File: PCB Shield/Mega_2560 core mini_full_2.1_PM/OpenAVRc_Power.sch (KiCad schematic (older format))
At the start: 18 parts, among them P17 BATT, P21 Sw_power, P26 LCD_Alim, P29 Sw_On, P30 MiniDCDC3A, U4 PM5033, U5 LD1117S33TR

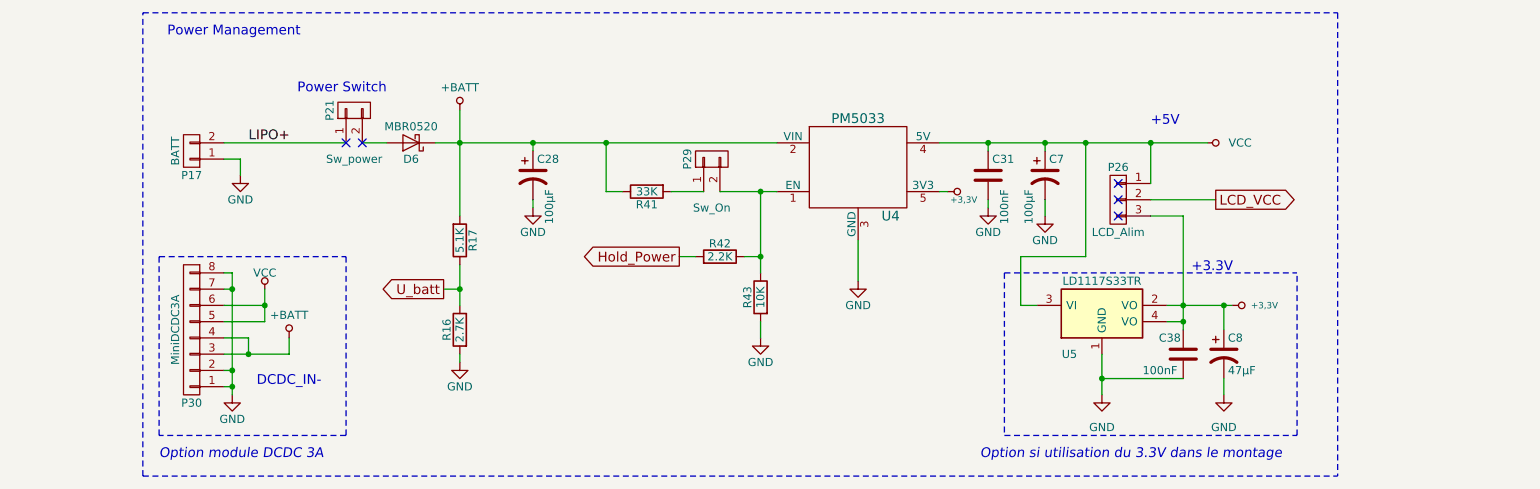
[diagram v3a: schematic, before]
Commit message: Update schematic & pcb files
add mosfet function
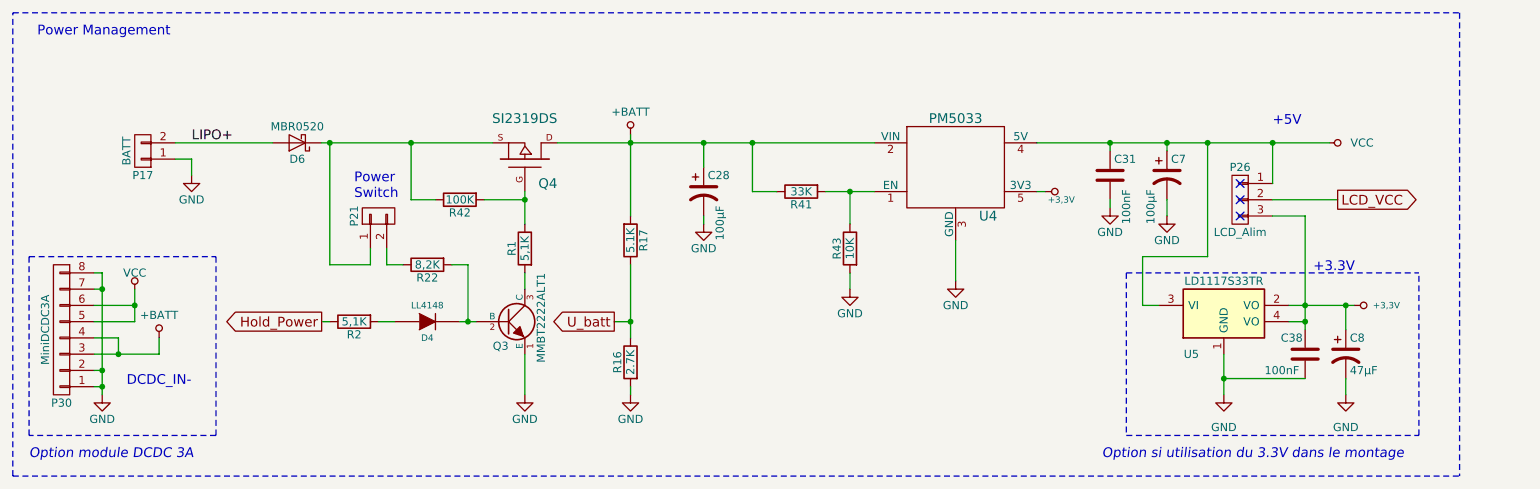
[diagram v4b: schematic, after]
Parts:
- removed P29: Sw_On, Pin_Headers:Pin_Header_Straight_1x02_Pitch2.54mm, symbol CONN_01X02
- added D4: LL4148, Diodes_SMD:D_SOD-123, symbol DIODE
- added Q3: MMBT2222ALT1, SOT-23_MMBT2222, symbol NPN
- added Q4: SI2319DS, SOT-23_MOS_P, symbol MOS_P
- added R1, R2: 5,1K, Resistors_SMD:R_1206, symbol R-RESCUE-Mega_2560_core_mini_full_2.0
- added R22: 8,2K, Resistors_SMD:R_1206, symbol R-RESCUE-Mega_2560_core_mini_full_2.0
- R42: value 2.2K -> 100K
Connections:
- net +BATT: now also Q4.D; no longer D6.1 (K)
- net GND: now also Q3.1 (E)
- net Hold_Power: now also R2.1; no longer R42.2
- net LIPO+: now also D6.2 (A); no longer P21.1 (P1)
- net at P21.2 (P2): now also R22.1; no longer D6.2 (A)
- net at R43.1, U4.1 (EN): now also R41.2; no longer R42.1
- new net: D6.1 (K), P21.1 (P1), Q4.S, R42.1
- new net: Q4.G, R1.1, R42.2
- new net: D4.2 (K), Q3.2 (B), R22.2
- new net: Q3.3 (C), R1.2
- new net: D4.1 (A), R2.2
- no-connect marks 5 -> 3
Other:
- note added: "Power\nSwitch"
- note removed: "Power Switch"
- moved on the sheet: C28, C31, C38, C7, C8, D6, P17, P21, P26, P30, R16, R17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

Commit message: Update pcb shield
Update core component (change pin 99 from GND to AGND).
Remove GND on AGND pin.
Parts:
- P30: footprint MiniDCDC3A -> v2.1:MiniDCDC3A
- Q3: footprint SOT-23_MMBT2222 -> v2.1:SOT-23_MMBT2222
- Q4: footprint SOT-23_MOS_P -> v2.1:SOT-23_MOS_P
- U4: footprint PM5033_SIL5 -> v2.1:Pm5033_sil5
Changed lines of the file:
@@
 Sheet 7 7
 Title "Shield Mega2560 core Full"
-Date "2018-04-19"
+Date "2018-04-25"
 Rev "2.10"
 Comp "© Team OpenAVRc"
@@
 $EndComp
 $Comp
-L GND-RESCUE-Mega_2560_core_mini_full_2.0 #PWR0110
+L GND-RESCUE-Mega_2560_core_mini_full_2.0 #PWR0109
 U 1 1 59C5313F
 P 8950 4550
-F 0 "#PWR0110" H 8950 4300 50  0001 C CNN
+F 0 "#PWR0109" H 8950 4300 50  0001 C CNN
 F 1 "GND" H 8950 4350 50  0000 C CNN
 F 2 "" H 8950 4550 50  0000 C CNN
@@
 +5V
 $Comp
-L VCC #PWR0111
+L VCC #PWR0110
 U 1 1 59C5314F
 P 9600 3000
-F 0 "#PWR0111" H 9600 2850 50  0001 C CNN
+F 0 "#PWR0110" H 9600 2850 50  0001 C CNN
 F 1 "VCC" V 9600 3200 50  0000 C CNN
 F 2 "" H 9600 3000 50  0000 C CNN
@@
 Power Management
 $Comp
-L GND-RESCUE-Mega_2560_core_mini_full_2.0 #PWR0112
+L GND-RESCUE-Mega_2560_core_mini_full_2.0 #PWR0111
 U 1 1 59C5315D
 P 7300 3850
-F 0 "#PWR0112" H 7300 3600 50  0001 C CNN
+F 0 "#PWR0111" H 7300 3600 50  0001 C CNN
 F 1 "GND" H 7300 3700 50  0000 C CNN
 F 2 "" H 7300 3850 50  0000 C CNN
@@
 $EndComp
 $Comp
-L GND-RESCUE-Mega_2560_core_mini_full_2.0 #PWR0113
+L GND-RESCUE-Mega_2560_core_mini_full_2.0 #PWR0112
 U 1 1 59C53163
 P 5300 4550
-F 0 "#PWR0113" H 5300 4300 50  0001 C CNN
+F 0 "#PWR0112" H 5300 4300 50  0001 C CNN
 F 1 "GND" H 5300 4400 50  0000 C CNN
 F 2 "" H 5300 4550 50  0000 C CNN
@@
 $EndComp
 $Comp
-L GND-RESCUE-Mega_2560_core_mini_full_2.0 #PWR0114
+L GND-RESCUE-Mega_2560_core_mini_full_2.0 #PWR0113
 U 1 1 59C53189
 P 8250 3400
-F 0 "#PWR0114" H 8250 3150 50  0001 C CNN
+F 0 "#PWR0113" H 8250 3150 50  0001 C CNN
 F 1 "GND" H 8250 3250 50  0000 C CNN
 F 2 "" H 8250 3400 50  0000 C CNN
@@
 $EndComp
 $Comp
-L GND-RESCUE-Mega_2560_core_mini_full_2.0 #PWR0115
+L GND-RESCUE-Mega_2560_core_mini_full_2.0 #PWR0114
 U 1 1 59C53196
 P 5750 3500
-F 0 "#PWR0115" H 5750 3250 50  0001 C CNN
+F 0 "#PWR0114" H 5750 3250 50  0001 C CNN
 F 1 "GND" H 5750 3350 50  0000 C CNN
 F 2 "" H 5750 3500 50  0000 C CNN
@@
 $EndComp
 $Comp
-L GND-RESCUE-Mega_2560_core_mini_full_2.0 #PWR0116
+L GND-RESCUE-Mega_2560_core_mini_full_2.0 #PWR0115
 U 1 1 59C531AC
 P 8600 3450
-F 0 "#PWR0116" H 8600 3200 50  0001 C CNN
+F 0 "#PWR0115" H 8600 3200 50  0001 C CNN
 F 1 "GND" H 8600 3300 50  0000 C CNN
 F 2 "" H 8600 3450 50  0000 C CNN
@@
 $EndComp
 $Comp
-L GND-RESCUE-Mega_2560_core_mini_full_2.0 #PWR0117
+L GND-RESCUE-Mega_2560_core_mini_full_2.0 #PWR0116
 U 1 1 59C531B9
 P 9700 4550
-F 0 "#PWR0117" H 9700 4300 50  0001 C CNN
+F 0 "#PWR0116" H 9700 4300 50  0001 C CNN
 F 1 "GND" H 9700 4350 50  0000 C CNN
 F 2 "" H 9700 4550 50  0000 C CNN
@@
 F 0 "P30" H 1800 4600 50  0000 C CNN
 F 1 "MiniDCDC3A" V 1900 4150 50  0000 C CNN
-F 2 "MiniDCDC3A" H 1800 4150 50  0001 C CNN
+F 2 "v2.1:MiniDCDC3A" H 1800 4150 50  0001 C CNN
 F 3 "" H 1800 4150 50  0000 C CNN
 	1    1800 4150
@@
 $EndComp
 $Comp
-L GND-RESCUE-Mega_2560_core_mini_full_2.0 #PWR0118
+L GND-RESCUE-Mega_2560_core_mini_full_2.0 #PWR0117
 U 1 1 59C531C8
 P 2050 4550
-F 0 "#PWR0118" H 2050 4300 50  0001 C CNN
+F 0 "#PWR0117" H 2050 4300 50  0001 C CNN
 F 1 "GND" H 2050 4400 50  0000 C CNN
 F 2 "" H 2050 4550 50  0000 C CNN
@@
 $EndComp
 $Comp
-L VCC #PWR0119
+L VCC #PWR0118
 U 1 1 59C531CE
 P 2250 3900
-F 0 "#PWR0119" H 2250 3750 50  0001 C CNN
+F 0 "#PWR0118" H 2250 3750 50  0001 C CNN
 F 1 "VCC" H 2250 4000 50  0000 C CNN
 F 2 "" H 2250 3900 50  0000 C CNN
@@
 $EndComp
 $Comp
-L GND-RESCUE-Mega_2560_core_mini_full_2.0 #PWR0120
+L GND-RESCUE-Mega_2560_core_mini_full_2.0 #PWR0119
 U 1 1 59C531DF
 P 2600 3200
-F 0 "#PWR0120" H 2600 2950 50  0001 C CNN
+F 0 "#PWR0119" H 2600 2950 50  0001 C CNN
 F 1 "GND" H 2600 3050 50  0000 C CNN
 F 2 "" H 2600 3200 50  0000 C CNN
@@
 Option module DCDC 3A
 $Comp
-L +BATT #PWR0121
+L +BATT #PWR0120
 U 1 1 59C53200
 P 5300 2950
-F 0 "#PWR0121" H 5300 2800 50  0001 C CNN
+F 0 "#PWR0120" H 5300 2800 50  0001 C CNN
 F 1 "+BATT" H 5300 3090 50  0000 C CNN
 F 2 "" H 5300 2950 50  0000 C CNN
@@
 LCD_VCC
 $Comp
-L +3,3V #PWR0122
+L +3,3V #PWR0121
 U 1 1 59CA5551
 P 9750 4000
-F 0 "#PWR0122" H 9750 3960 30  0001 C CNN
+F 0 "#PWR0121" H 9750 3960 30  0001 C CNN
 F 1 "+3,3V" V 9750 4200 39  0000 C CNN
 F 2 "" H 9750 4000 60  0001 C CNN
@@
 F 0 "U4" H 7500 2850 60  0000 C CNN
 F 1 "PM5033" H 7300 3450 60  0000 C CNN
-F 2 "PM5033_SIL5" H 7300 3150 60  0001 C CNN
+F 2 "v2.1:Pm5033_sil5" H 7300 3150 60  0001 C CNN
 F 3 "" H 7300 3150 60  0000 C CNN
 	1    7300 3150
@@
 $EndComp
 $Comp
-L +3,3V #PWR0123
+L +3,3V #PWR0122
 U 1 1 59FED94A
 P 7850 3300
-F 0 "#PWR0123" H 7850 3260 30  0001 C CNN
+F 0 "#PWR0122" H 7850 3260 30  0001 C CNN
 F 1 "+3,3V" V 7900 3400 39  0000 C CNN
 F 2 "" H 7850 3300 60  0001 C CNN
@@
 $EndComp
 $Comp
-L GND-RESCUE-Mega_2560_core_mini_full_2.0 #PWR0124
+L GND-RESCUE-Mega_2560_core_mini_full_2.0 #PWR0123
 U 1 1 5A0873AD
 P 6650 3900
-F 0 "#PWR0124" H 6650 3650 50  0001 C CNN
+F 0 "#PWR0123" H 6650 3650 50  0001 C CNN
 F 1 "GND" H 6650 3750 50  0000 C CNN
 F 2 "" H 6650 3900 50  0000 C CNN
@@
 $EndComp
 $Comp
-L +BATT #PWR0125
+L +BATT #PWR0124
 U 1 1 5A702E5A
 P 2400 4200
-F 0 "#PWR0125" H 2400 4050 50  0001 C CNN
+F 0 "#PWR0124" H 2400 4050 50  0001 C CNN
 F 1 "+BATT" H 2400 4340 50  0000 C CNN
 F 2 "" H 2400 4200 50  0000 C CNN
@@
 F 0 "Q4" V 4500 3300 60  0000 R CNN
 F 1 "SI2319DS" V 4900 3300 60  0000 R CNN
-F 2 "SOT-23_MOS_P" H 4650 3100 60  0001 C CNN
+F 2 "v2.1:SOT-23_MOS_P" H 4650 3100 60  0001 C CNN
 F 3 "" H 4650 3100 60  0000 C CNN
 	1    4650 3100
@@
 F 0 "Q3" H 4550 3950 50  0000 R CNN
 F 1 "MMBT2222ALT1" V 4750 4400 50  0000 R CNN
-F 2 "SOT-23_MMBT2222" H 4550 4100 60  0001 C CNN
+F 2 "v2.1:SOT-23_MMBT2222" H 4550 4100 60  0001 C CNN
 F 3 "" H 4550 4100 60  0000 C CNN
 	1    4550 4100
@@
 $EndComp
 $Comp
-L GND-RESCUE-Mega_2560_core_mini_full_2.0 #PWR0126
+L GND-RESCUE-Mega_2560_core_mini_full_2.0 #PWR0125
 U 1 1 5AA6A33E
 P 4650 4550
-F 0 "#PWR0126" H 4650 4300 50  0001 C CNN
+F 0 "#PWR0125" H 4650 4300 50  0001 C CNN
 F 1 "GND" H 4650 4400 50  0000 C CNN
 F 2 "" H 4650 4550 50  0000 C CNN
